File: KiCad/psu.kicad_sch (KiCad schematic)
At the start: 25 parts, among them J1 Conn_02x04_Top_Bottom, J2 ATX-24, U1 FP6385, U2 FP6385

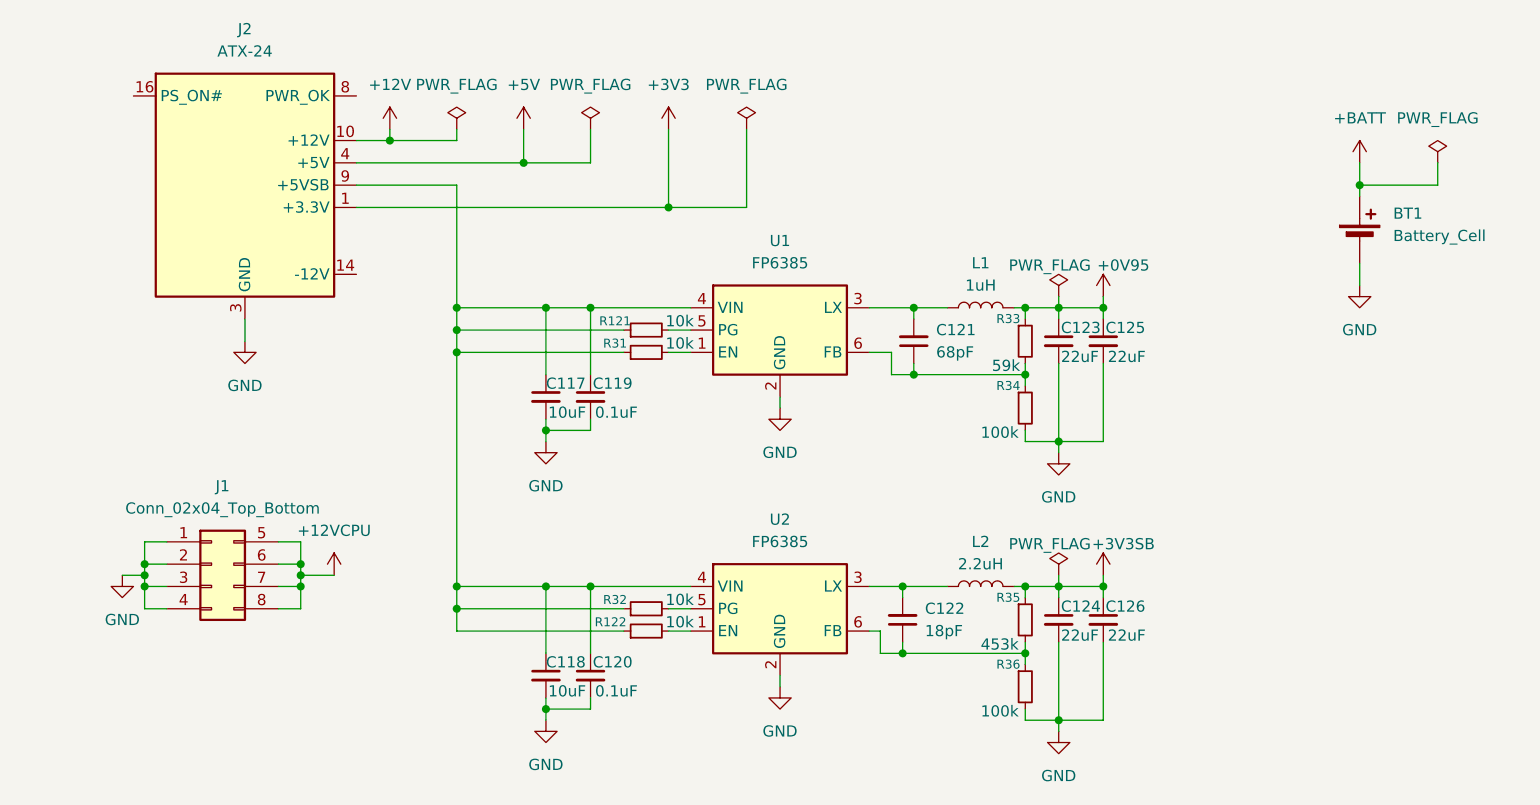
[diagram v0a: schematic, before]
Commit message: Add programming header and power and reset switches
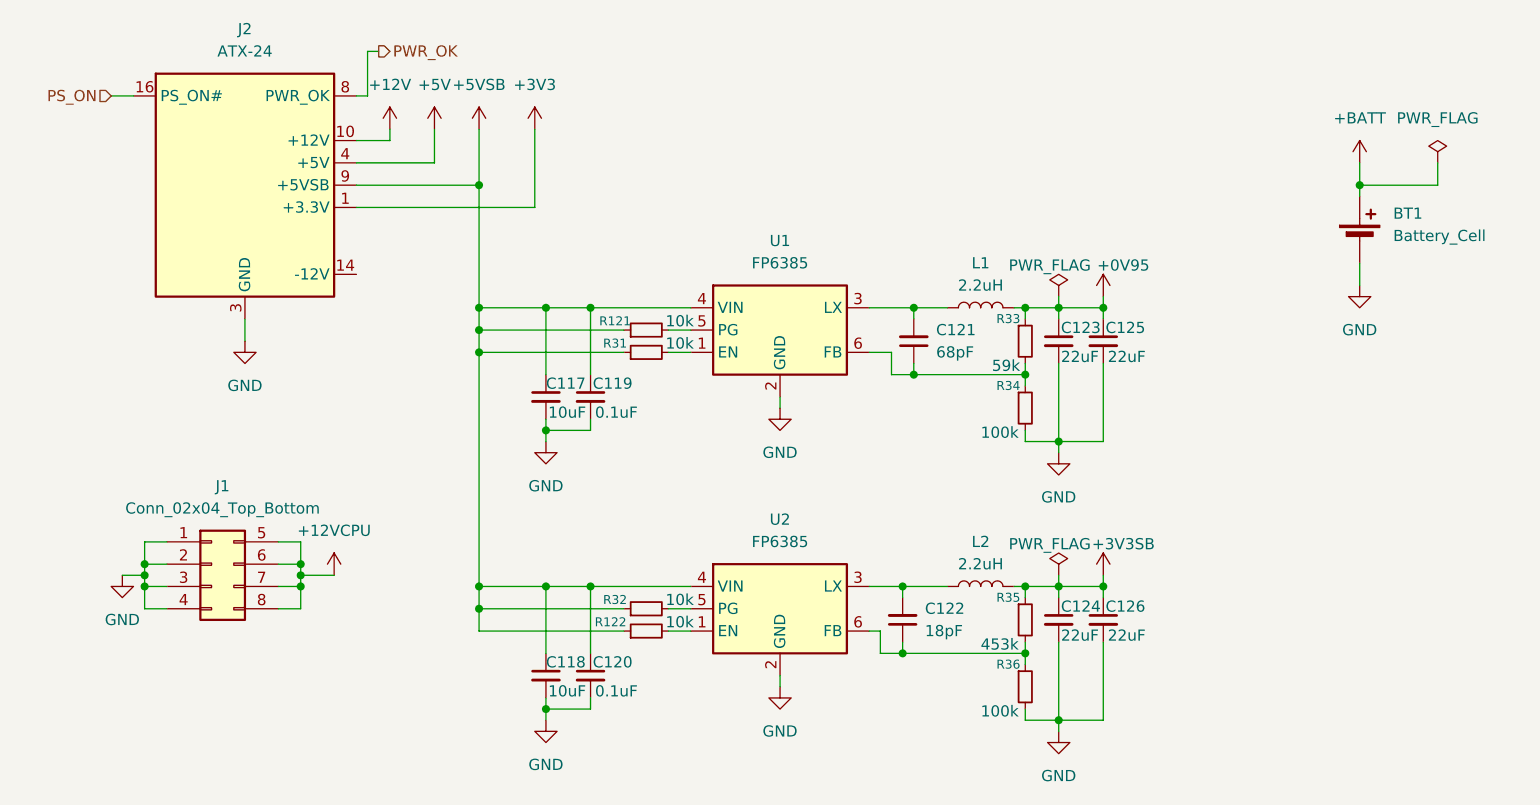
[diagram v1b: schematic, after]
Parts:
- L1: value 1uH -> 2.2uH
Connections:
- net +5VSB: now reaches C117.1, C118.1, C119.1, C120.1, J2.9 (+5VSB), R121.1, R122.1, R31.1, R32.1, U1.4 (VIN), U2.4 (VIN)
- net PS_ON: now reaches J2.16 (PS_ON#)
- net PWR_OK: now reaches J2.8 (PWR_OK)

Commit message: Remove 0.95V Power Supply, Replace 3.3V Standby Power Supply
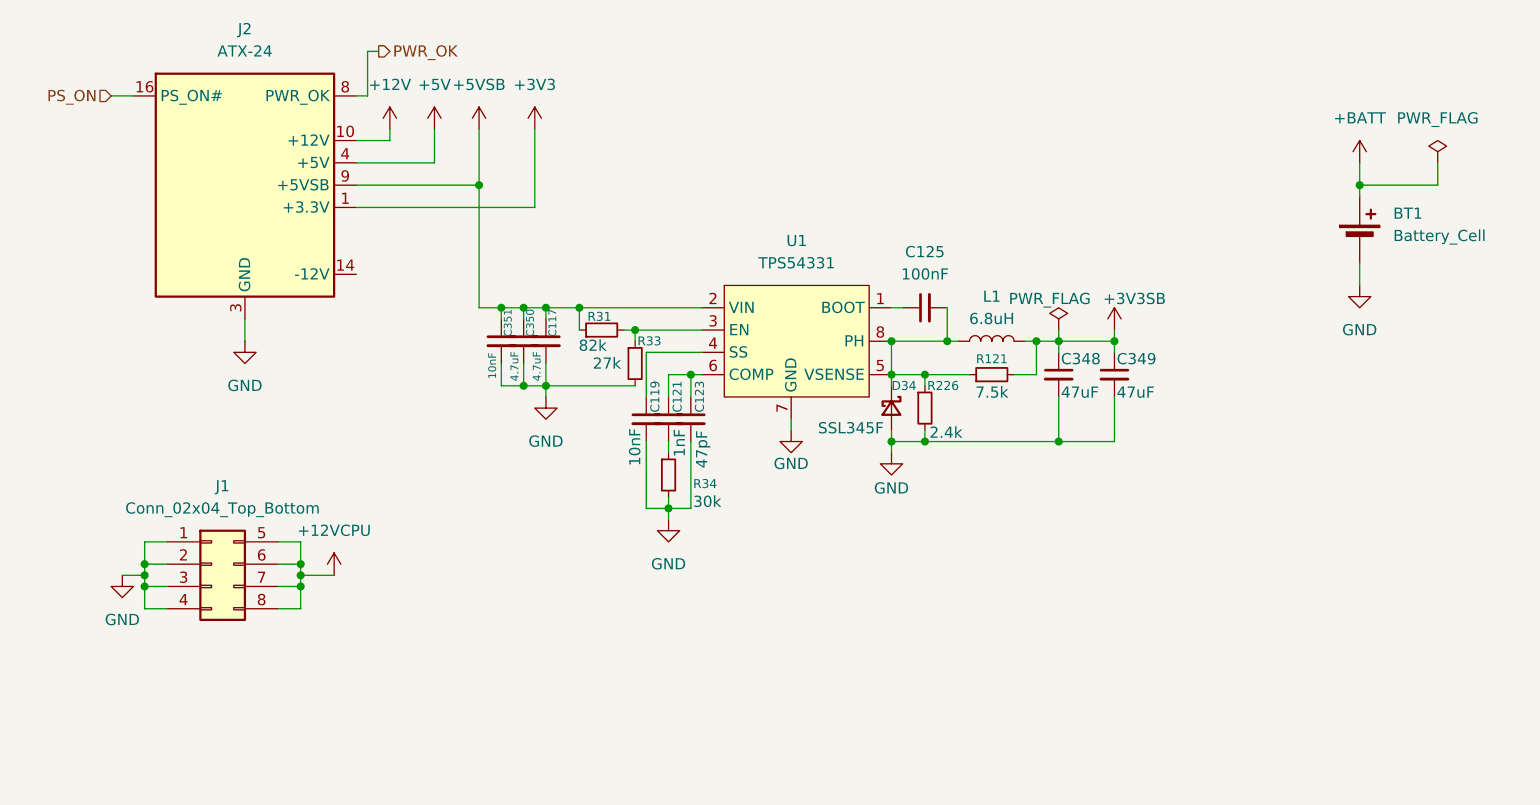
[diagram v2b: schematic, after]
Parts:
- removed C118: 10uF, symbol Device:C_Small
- removed C120: 0.1uF, symbol Device:C_Small
- removed C122: 18pF, symbol Device:C_Small
- removed C124, C126: 22uF, symbol Device:C_Small
- removed L2: 2.2uH, symbol Device:L
- removed R122, R32: 10k, symbol Device:R_Small
- removed R35: 453k, symbol Device:R_Small
- removed R36: 100k, symbol Device:R_Small
- removed U1, U2: FP6385, Package_TO_SOT_SMD:SOT-23-6, symbol Regulator_Switching:TPS563200
- added C348, C349: 47uF, symbol Device:C_Small
- added C350: 4.7uF, symbol Device:C_Small
- added C351: 10nF, symbol Device:C_Small
- added D34: SSL345F, symbol Device:D_Schottky_Small
- added R226: 2.4k, symbol Device:R_Small
- added U1: TPS54331, Package_SO:SOIC-8_3.9x4.9mm_P1.27mm, symbol custom:TPS54331
- C117: value 10uF -> 4.7uF
- C119: value 0.1uF -> 10nF
- C121: value 68pF -> 1nF
- C123: value 22uF -> 47pF
- C125: value 22uF -> 100nF
- L1: value 2.2uH -> 6.8uH
- R121: value 10k -> 7.5k
- R31: value 10k -> 82k
- R33: value 59k -> 27k
- R34: value 100k -> 30k
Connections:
- net +3V3SB: now also L1.2, R121.2, C348.1, C349.1
- net +5VSB: now also C350.1, C351.1, U1.2 (VIN); no longer C119.1, R121.1
- net GND: now also R33.2, C348.2, C349.2, C350.2, C351.2, D34.2 (A), R226.2, U1.7 (GND); no longer C125.2
- net at R31.2: now also R33.1, U1.3 (EN)
- net at L1.1: now also C125.2, R121.1, D34.1 (K), R226.1, U1.5 (VSENSE), U1.8 (PH); no longer C121.2
- removed net +0V95: C123.1, C125.1, L1.2, R33.1
- new net: C125.1, U1.1 (BOOT)
- new net: C119.1, U1.4 (SS)
- new net: C121.1, C123.1, U1.6 (COMP)
- new net: C121.2, R34.1

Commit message: Work though ERC errors
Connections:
- no-connect marks 0 -> 1
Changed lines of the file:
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@@
+	)
+	(junction
+		(at 58.42 106.68)
+		(diameter 0)
+		(color 0 0 0 0)
 	)
 	(junction
@@
 	)
 	(junction
+		(at 58.42 114.3)
+		(diameter 0)
+		(color 0 0 0 0)
+	)
+	(junction
 		(at 81.28 80.01)
 		(diameter 0)
 		(color 0 0 0 0)
 	)
-	(junction
-		(at 58.42 110.49)
-		(diameter 0)
-		(color 0 0 0 0)
+	(no_connect
+		(at 64.77 76.2)
 	)
 	(wire
@@
 	(wire
 		(pts
+			(xy 58.42 105.41) (xy 58.42 106.68)
+		)
+		(stroke
+			(width 0)
+			(type default)
+		)
+	)
+	(wire
+		(pts
 			(xy 40.64 111.76) (xy 40.64 110.49)
 		)
@@
 	(wire
 		(pts
-			(xy 58.42 109.22) (xy 58.42 110.49)
+			(xy 58.42 109.22) (xy 58.42 111.76)
 		)
 		(stroke
@@
 	(wire
 		(pts
+			(xy 58.42 115.57) (xy 58.42 114.3)
+		)
+		(stroke
+			(width 0)
+			(type default)
+		)
+	)
+	(wire
+		(pts
 			(xy 132.08 83.82) (xy 133.35 83.82)
 		)
@@
 	(wire
 		(pts
+			(xy 58.42 106.68) (xy 58.42 109.22)
+		)
+		(stroke
+			(width 0)
+			(type default)
+		)
+	)
+	(wire
+		(pts
 			(xy 83.82 88.9) (xy 86.36 88.9)
 		)
@@
 	(wire
 		(pts
-			(xy 58.42 106.68) (xy 58.42 109.22)
-		)
-		(stroke
-			(width 0)
-			(type default)
-		)
-	)
-	(wire
-		(pts
 			(xy 66.04 55.88) (xy 66.04 50.8)
 		)
@@
 	(wire
 		(pts
-			(xy 58.42 110.49) (xy 62.23 110.49)
-		)
-		(stroke
-			(width 0)
-			(type default)
-		)
-	)
-	(wire
-		(pts
 			(xy 43.18 106.68) (xy 40.64 106.68)
 		)
@@
 		(pts
 			(xy 179.07 63.5) (xy 179.07 66.04)
-		)
-		(stroke
-			(width 0)
-			(type default)
-		)
-	)
-	(wire
-		(pts
-			(xy 58.42 111.76) (xy 58.42 110.49)
 		)
 		(stroke
@@
 	(symbol
 		(lib_id "custom:+12VCPU")
-		(at 62.23 110.49 0)
+		(at 58.42 105.41 0)
 		(unit 1)
 		(exclude_from_sim no)
@@
 		(fields_autoplaced yes)
 		(property "Reference" "#PWR037"
-			(at 62.23 114.3 0)
+			(at 58.42 109.22 0)
 			(effects
 				(font
@@
 		)
 		(property "Value" "+12VCPU"
-			(at 62.23 105.41 0)
+			(at 58.42 100.33 0)
 			(effects
 				(font
@@
 		)
 		(property "Footprint" ""
-			(at 62.23 110.49 0)
+			(at 58.42 105.41 0)
 			(effects
 				(font
@@
 		)
 		(property "Datasheet" ""
-			(at 62.23 110.49 0)
+			(at 58.42 105.41 0)
 			(effects
 				(font
@@
 		)
 		(property "Description" "Power symbol creates a global label with name \"+12VCPU\""
-			(at 62.23 110.49 0)
+			(at 58.42 105.41 0)
 			(effects
 				(font
@@
 	)
 	(symbol
+		(lib_id "power:PWR_FLAG")
+		(at 58.42 115.57 180)
+		(unit 1)
+		(exclude_from_sim no)
+		(in_bom yes)
+		(on_board yes)
+		(dnp no)
+		(fields_autoplaced yes)
+		(property "Reference" "#FLG04"
+			(at 58.42 117.475 0)
+			(effects
+				(font
+					(size 1.27 1.27)
+				)
+				(hide yes)
+			)
+		)
+		(property "Value" "PWR_FLAG"
+			(at 58.42 120.65 0)
+			(effects
+				(font
+					(size 1.27 1.27)
+				)
+			)
+		)
+		(property "Footprint" ""
+			(at 58.42 115.57 0)
+			(effects
+				(font
+					(size 1.27 1.27)
+				)
+				(hide yes)
+			)
+		)
+		(property "Datasheet" "~"
+			(at 58.42 115.57 0)
+			(effects
+				(font
+					(size 1.27 1.27)
+				)
+				(hide yes)
+			)
+		)
+		(property "Description" "Special symbol for telling ERC where power comes from"
+			(at 58.42 115.57 0)
+			(effects
+				(font
+					(size 1.27 1.27)
+				)
+				(hide yes)
+			)
+		)
+		(pin "1"
+		)
+		(instances
+			(project ""
+				(path "/49abeb3a-c598-45a3-ba6b-595eb04f17a8/73807de7-58af-4eca-b212-2dba82ac67f9"
+					(reference "#FLG04")
+					(unit 1)
+				)
+			)
+		)
+	)
+	(symbol
 		(lib_id "Device:C_Small")
 		(at 102.87 92.71 0)
@@
 		(on_board yes)
 		(dnp no)
-		(fields_autoplaced yes)
 		(property "Reference" "J1"
 			(at 49.53 100.33 0)
@@
 		)
 		(property "Value" "Conn_02x04_Top_Bottom"
-			(at 49.53 102.87 0)
-			(effects
-				(font
+			(at 39.624 103.124 0)
+			(effects
+				(font

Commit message: Re-annotate components
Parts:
- renumbered C351 to C130, C350 to C131, C117 to C132, C119 to C133, C121 to C134, C123 to C135, C125 to C136, C348 to C137, C349 to C138, D34 to D21, R33 to R100, R34 to R101, R226 to R102, R121 to R103, R31 to R99, U1 to U6

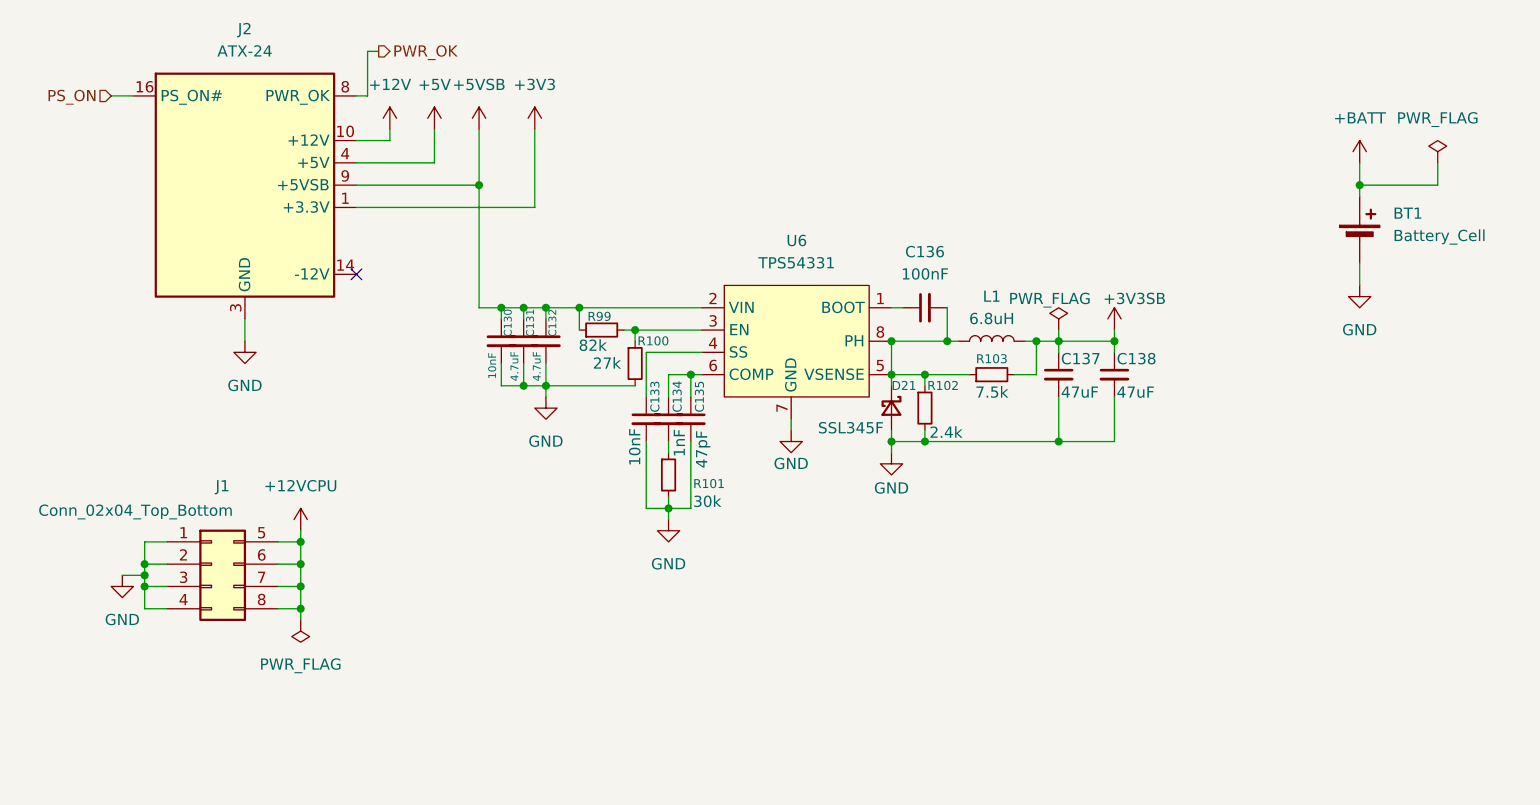
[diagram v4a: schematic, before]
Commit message: Add TVS diodes for ESD protection
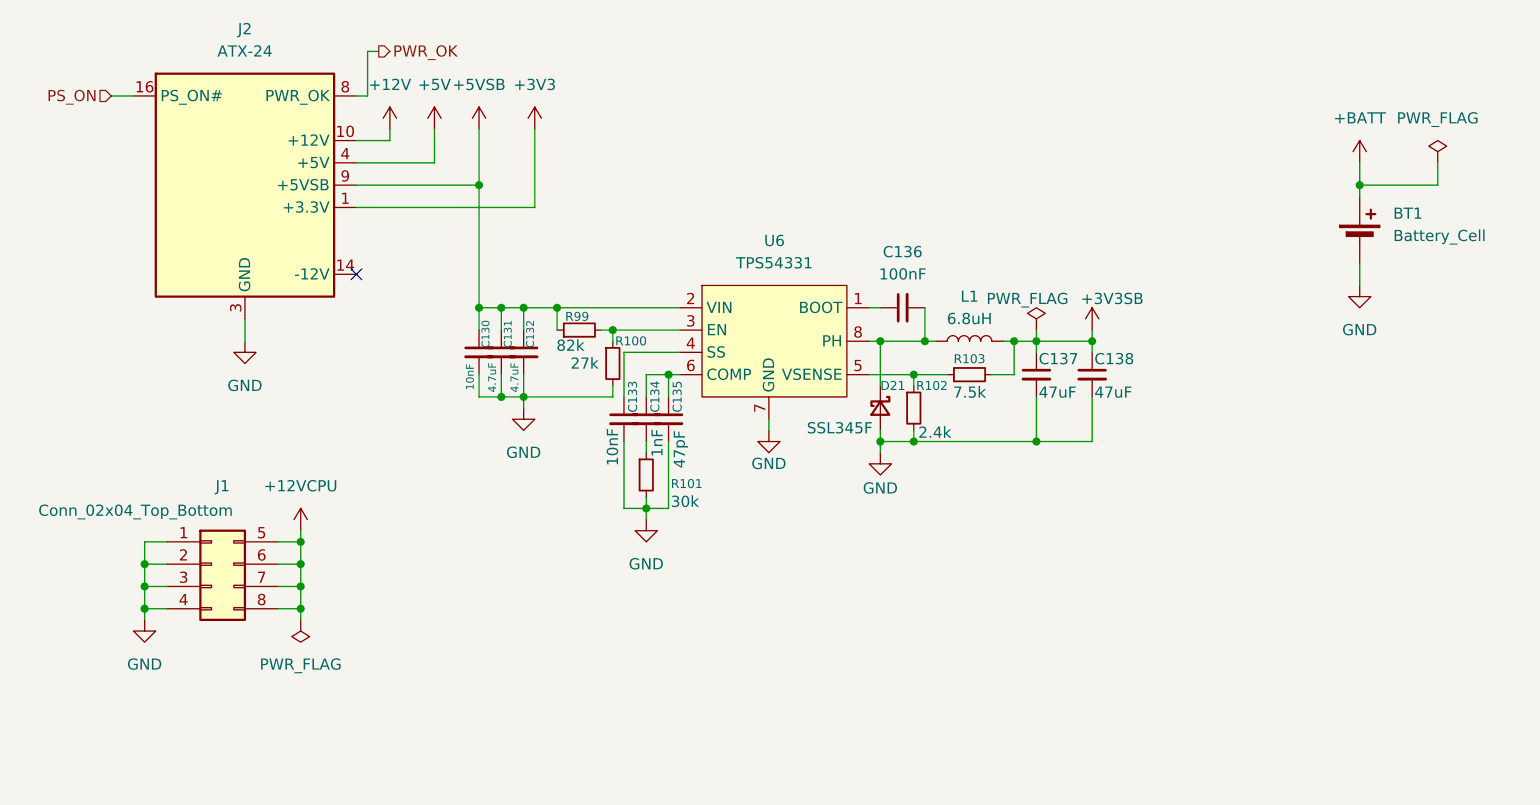
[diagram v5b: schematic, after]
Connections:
- net at C136.2, D21.1 (K), L1.1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: no longer R102.1, R103.1, U6.5 (VSENSE)
- new net: R102.1, R103.1, U6.5 (VSENSE)
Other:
- moved on the sheet: C130, C131, C132, C133, C134, C135, C136, C137, C138, D21, L1, R100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

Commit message: Add USB Type E Header Footprint
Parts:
- U6: symbol custom:TPS54331 -> Custom:TPS54331
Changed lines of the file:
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@@
 	)
 	(symbol
-		(lib_id "custom:TPS54331")
+		(lib_id "Custom:TPS54331")
 		(at 111.76 76.2 0)
 		(unit 1)

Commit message: Add more footprints
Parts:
- BT1: footprint (none) -> EasyEDA2KiCAD:BAT-TH_BH-123A-A5BJ002
- C130, C131, C132, C133, C134, C135, C136: footprint (none) -> Capacitor_SMD:C_0603_1608Metric
- C137, C138: footprint (none) -> Capacitor_SMD:C_0805_2012Metric
- J2: footprint (none) -> Connector_Molex:Molex_Mini-Fit_Jr_5566-24A_2x12_P4.20mm_Vertical
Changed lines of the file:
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@@
 			)
 		)
-		(property "Footprint" ""
+		(property "Footprint" "EasyEDA2KiCAD:BAT-TH_BH-123A-A5BJ002"
 			(at 179.07 70.866 90)
 			(effects
@@
 			)
 		)
-		(property "Footprint" ""
+		(property "Footprint" "Capacitor_SMD:C_0805_2012Metric"
 			(at 148.59 87.63 0)
 			(effects
@@
 			)
 		)
-		(property "Footprint" ""
+		(property "Footprint" "Capacitor_SMD:C_0603_1608Metric"
 			(at 127 80.01 0)
 			(effects
@@
 			)
 		)
-		(property "Footprint" ""
+		(property "Footprint" "Capacitor_SMD:C_0603_1608Metric"
 			(at 95.25 92.71 0)
 			(effects
@@
 			)
 		)
-		(property "Footprint" ""
+		(property "Footprint" "Capacitor_SMD:C_0603_1608Metric"
 			(at 100.33 92.71 0)
 			(effects
@@
 			)
 		)
-		(property "Footprint" ""
+		(property "Footprint" "Capacitor_SMD:C_0603_1608Metric"
 			(at 78.74 85.09 0)
 			(effects
@@
 			)
 		)
-		(property "Footprint" ""
+		(property "Footprint" "Capacitor_SMD:C_0805_2012Metric"
 			(at 142.24 87.63 0)
 			(effects
@@
 			)
 		)
-		(property "Footprint" ""
+		(property "Footprint" "Capacitor_SMD:C_0603_1608Metric"
 			(at 83.82 85.09 0)
 			(effects
@@
 			)
 		)
-		(property "Footprint" ""
+		(property "Footprint" "Capacitor_SMD:C_0603_1608Metric"
 			(at 81.28 85.09 0)
 			(effects
@@
 			)
 		)
-		(property "Footprint" ""
+		(property "Footprint" "Connector_Molex:Molex_Mini-Fit_Jr_5566-24A_2x12_P4.20mm_Vertical"
 			(at 52.07 68.58 0)
 			(effects
@@
 			)
 		)
-		(property "Footprint" ""
+		(property "Footprint" "Capacitor_SMD:C_0603_1608Metric"
 			(at 97.79 92.71 0)
 			(effects
